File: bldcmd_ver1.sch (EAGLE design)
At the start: 26 parts, among them IC1 STSPIN32F0, Q1 PSMN2R4-30MLD, Q2 PSMN2R4-30MLD, Q3 PSMN2R4-30MLD, Q4 PSMN2R4-30MLD, Q5 PSMN2R4-30MLD, Q6 PSMN2R4-30MLD

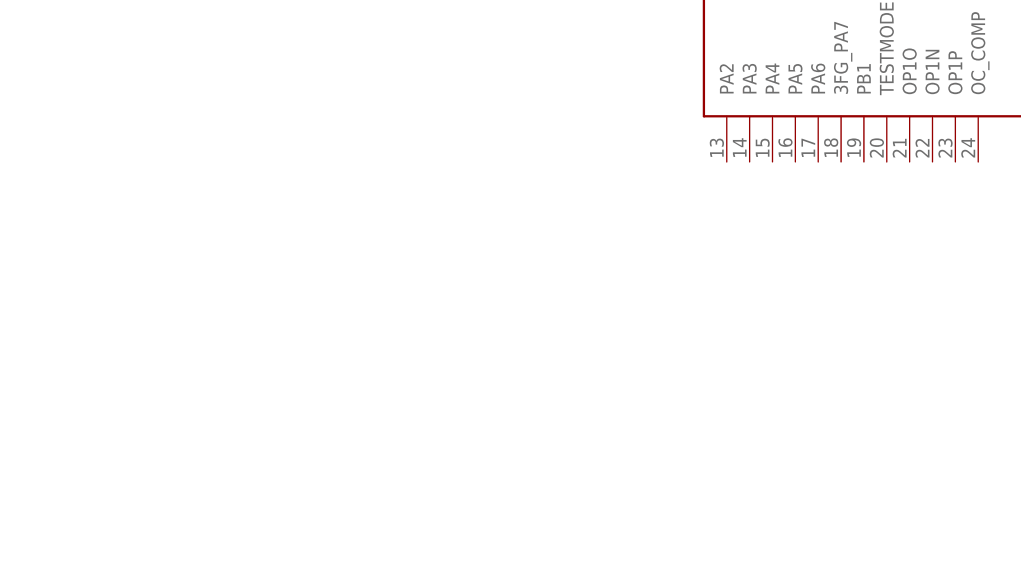
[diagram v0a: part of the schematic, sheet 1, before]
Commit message: 磁気エンコーダAS5047P追加
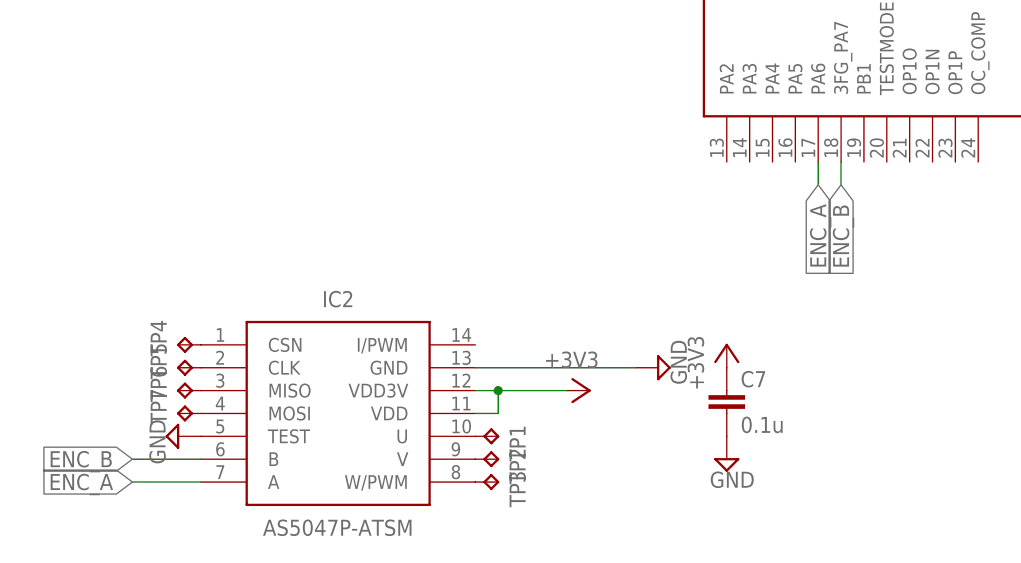
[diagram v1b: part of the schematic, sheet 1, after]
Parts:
- added C7: 0.1u, rcl:C-EUC0603K
- added IC2: AS5047P-ATSM, rcssl_lib:AS5047P-ATSM
- added TP1, TP2, TP3, TP4, TP5, TP6, TP7: TPTP06R, testpad:TPTP06R
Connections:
- new net +3V3: C7.1, IC2.VDD, IC2.VDD3V
- new net ENC_A: IC1.PA6, IC2.A
- new net ENC_B: IC1.3FG_PA7, IC2.B
- new net N$12: IC2.MISO, TP6.TP
- new net N$17: IC2.MOSI, TP7.TP
- new net N$2: IC2.U, TP1.TP
- new net N$3: IC2.V, TP2.TP
- new net N$6: IC2.W/PWM, TP3.TP
- new net N$7: IC2.CSN, TP4.TP
- new net N$8: IC2.CLK, TP5.TP
- net GND: now also C7.2, IC2.GND, IC2.TEST
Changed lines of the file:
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@@
 <part name="R13" library="rcl" library_urn="urn:adsk.eagle:library:334" deviceset="R-EU_" device="R3216" package3d_urn="urn:adsk.eagle:package:23557/2" value="0.01"/>
 <part name="SUPPLY1" library="supply2" library_urn="urn:adsk.eagle:library:372" deviceset="GND" device=""/>
+<part name="IC2" library="rcssl_lib" deviceset="AS5047P-ATSM" device=""/>
+<part name="+3V1" library="supply1" library_urn="urn:adsk.eagle:library:371" deviceset="+3V3" device=""/>
+<part name="SUPPLY2" library="supply2" library_urn="urn:adsk.eagle:library:372" deviceset="GND" device=""/>
+<part name="C7" library="rcl" library_urn="urn:adsk.eagle:library:334" deviceset="C-EU" device="C0603K" package3d_urn="urn:adsk.eagle:package:23680/2" value="0.1u"/>
+<part name="+3V2" library="supply1" library_urn="urn:adsk.eagle:library:371" deviceset="+3V3" device=""/>
+<part name="SUPPLY3" library="supply2" library_urn="urn:adsk.eagle:library:372" deviceset="GND" device=""/>
+<part name="TP1" library="testpad" library_urn="urn:adsk.eagle:library:385" deviceset="TP" device="TP06R" package3d_urn="urn:adsk.eagle:package:27954/1"/>
+<part name="TP2" library="testpad" library_urn="urn:adsk.eagle:library:385" deviceset="TP" device="TP06R" package3d_urn="urn:adsk.eagle:package:27954/1"/>
+<part name="TP3" library="testpad" library_urn="urn:adsk.eagle:library:385" deviceset="TP" device="TP06R" package3d_urn="urn:adsk.eagle:package:27954/1"/>
+<part name="TP4" library="testpad" library_urn="urn:adsk.eagle:library:385" deviceset="TP" device="TP06R" package3d_urn="urn:adsk.eagle:package:27954/1"/>
+<part name="TP5" library="testpad" library_urn="urn:adsk.eagle:library:385" deviceset="TP" device="TP06R" package3d_urn="urn:adsk.eagle:package:27954/1"/>
+<part name="TP6" library="testpad" library_urn="urn:adsk.eagle:library:385" deviceset="TP" device="TP06R" package3d_urn="urn:adsk.eagle:package:27954/1"/>
+<part name="TP7" library="testpad" library_urn="urn:adsk.eagle:library:385" deviceset="TP" device="TP06R" package3d_urn="urn:adsk.eagle:package:27954/1"/>
+<part name="SUPPLY4" library="supply2" library_urn="urn:adsk.eagle:library:372" deviceset="GND" device=""/>
 </parts>
 <sheets>
@@
 <instance part="C2" gate="G$1" x="58.42" y="-12.7" rot="R90"/>
 <instance part="C3" gate="G$1" x="58.42" y="-22.86" rot="R90"/>
+<instance part="IC2" gate="G$1" x="-43.18" y="-71.12"/>
+<instance part="+3V1" gate="G$1" x="0" y="-76.2" rot="R270"/>
+<instance part="SUPPLY2" gate="GND" x="7.62" y="-73.66" rot="R90"/>
+<instance part="C7" gate="G$1" x="15.24" y="-76.2"/>
+<instance part="+3V2" gate="G$1" x="15.24" y="-71.12"/>
+<instance part="SUPPLY3" gate="GND" x="15.24" y="-83.82"/>
+<instance part="TP1" gate="G$1" x="-10.16" y="-81.28" rot="R270"/>
+<instance part="TP2" gate="G$1" x="-10.16" y="-83.82" rot="R270"/>
+<instance part="TP3" gate="G$1" x="-10.16" y="-86.36" rot="R270"/>
+<instance part="TP4" gate="G$1" x="-45.72" y="-71.12" rot="R90"/>
+<instance part="TP5" gate="G$1" x="-45.72" y="-73.66" rot="R90"/>
+<instance part="TP6" gate="G$1" x="-45.72" y="-76.2" rot="R90"/>
+<instance part="TP7" gate="G$1" x="-45.72" y="-78.74" rot="R90"/>
+<instance part="SUPPLY4" gate="GND" x="-45.72" y="-81.28" rot="R270"/>
 </instances>
 <busses>
@@
 </segment>
 </net>
+<net name="GND" class="0">
+<segment>
+<pinref part="IC2" gate="G$1" pin="GND"/>
+<pinref part="SUPPLY2" gate="GND" pin="GND"/>
+<wire x1="-12.7" y1="-73.66" x2="5.08" y2="-73.66" width="0.1524" layer="91"/>
+</segment>
+<segment>
+<pinref part="C7" gate="G$1" pin="2"/>
+<pinref part="SUPPLY3" gate="GND" pin="GND"/>
+</segment>
+<segment>
+<pinref part="IC2" gate="G$1" pin="TEST"/>
+<pinref part="SUPPLY4" gate="GND" pin="GND"/>
+</segment>
+</net>
+<net name="+3V3" class="0">
+<segment>
+<pinref part="IC2" gate="G$1" pin="VDD"/>
+<wire x1="-12.7" y1="-78.74" x2="-10.16" y2="-78.74" width="0.1524" layer="91"/>
+<wire x1="-10.16" y1="-78.74" x2="-10.16" y2="-76.2" width="0.1524" layer="91"/>
+<pinref part="IC2" gate="G$1" pin="VDD3V"/>
+<wire x1="-10.16" y1="-76.2" x2="-12.7" y2="-76.2" width="0.1524" layer="91"/>
+<pinref part="+3V1" gate="G$1" pin="+3V3"/>
+<wire x1="-10.16" y1="-76.2" x2="-2.54" y2="-76.2" width="0.1524" layer="91"/>
+<junction x="-10.16" y="-76.2"/>
+</segment>
+<segment>
+<pinref part="C7" gate="G$1" pin="1"/>
+<pinref part="+3V2" gate="G$1" pin="+3V3"/>
+</segment>
+</net>
+<net name="ENC_B" class="0">
+<segment>
+<pinref part="IC2" gate="G$1" pin="B"/>
+<wire x1="-43.18" y1="-83.82" x2="-50.8" y2="-83.82" width="0.1524" layer="91"/>
+<label x="-50.8" y="-83.82" size="1.778" layer="95" rot="R180" xref="yes"/>
+</segment>
+<segment>
+<pinref part="IC1" gate="G$1" pin="3FG_PA7"/>
+<wire x1="27.94" y1="-50.8" x2="27.94" y2="-53.34" width="0.1524" layer="91"/>
+<label x="27.94" y="-53.34" size="1.778" layer="95" rot="R270" xref="yes"/>
+</segment>
+</net>
+<net name="ENC_A" class="0">
+<segment>
+<pinref part="IC2" gate="G$1" pin="A"/>
+<wire x1="-43.18" y1="-86.36" x2="-50.8" y2="-86.36" width="0.1524" layer="91"/>
+<label x="-50.8" y="-86.36" size="1.778" layer="95" rot="R180" xref="yes"/>
+</segment>
+<segment>
+<pinref part="IC1" gate="G$1" pin="PA6"/>
+<wire x1="25.4" y1="-50.8" x2="25.4" y2="-53.34" width="0.1524" layer="91"/>
+<label x="25.4" y="-53.34" size="1.778" layer="95" rot="R270" xref="yes"/>
+</segment>
+</net>
+<net name="N$2" class="0">
+<segment>
+<pinref part="IC2" gate="G$1" pin="U"/>
+<pinref part="TP1" gate="G$1" pin="TP"/>
+</segment>
+</net>
+<net name="N$3" class="0">
+<segment>
+<pinref part="IC2" gate="G$1" pin="V"/>
+<pinref part="TP2" gate="G$1" pin="TP"/>
+</segment>
+</net>
+<net name="N$6" class="0">
+<segment>
+<pinref part="IC2" gate="G$1" pin="W/PWM"/>
+<pinref part="TP3" gate="G$1" pin="TP"/>
+</segment>
+</net>
+<net name="N$7" class="0">
+<segment>
+<pinref part="IC2" gate="G$1" pin="CSN"/>
+<pinref part="TP4" gate="G$1" pin="TP"/>
+</segment>
+</net>
+<net name="N$8" class="0">
+<segment>
+<pinref part="IC2" gate="G$1" pin="CLK"/>
+<pinref part="TP5" gate="G$1" pin="TP"/>
+</segment>
+</net>
+<net name="N$12" class="0">
+<segment>
+<pinref part="IC2" gate="G$1" pin="MISO"/>
+<pinref part="TP6" gate="G$1" pin="TP"/>
+</segment>
+</net>
+<net name="N$17" class="0">
+<segment>
+<pinref part="IC2" gate="G$1" pin="MOSI"/>
+<pinref part="TP7" gate="G$1" pin="TP"/>
+</segment>
+</net>

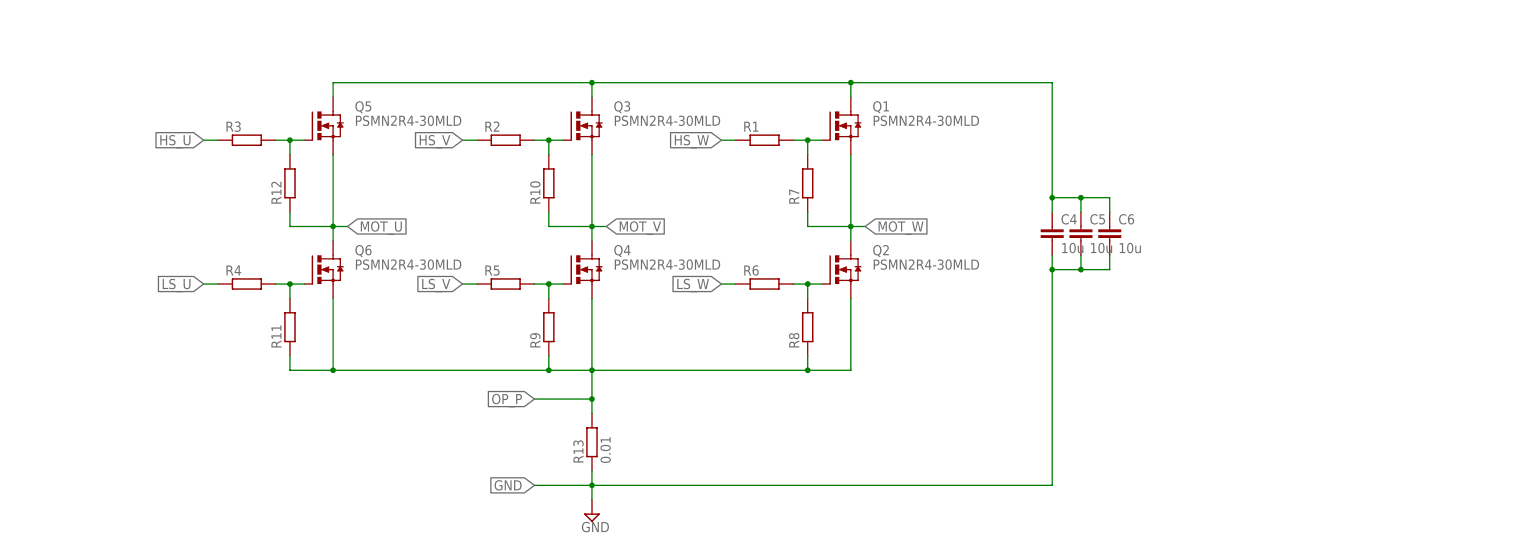
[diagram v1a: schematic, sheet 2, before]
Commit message: CスナバをGNDからローサイドFETのソースに接続変更
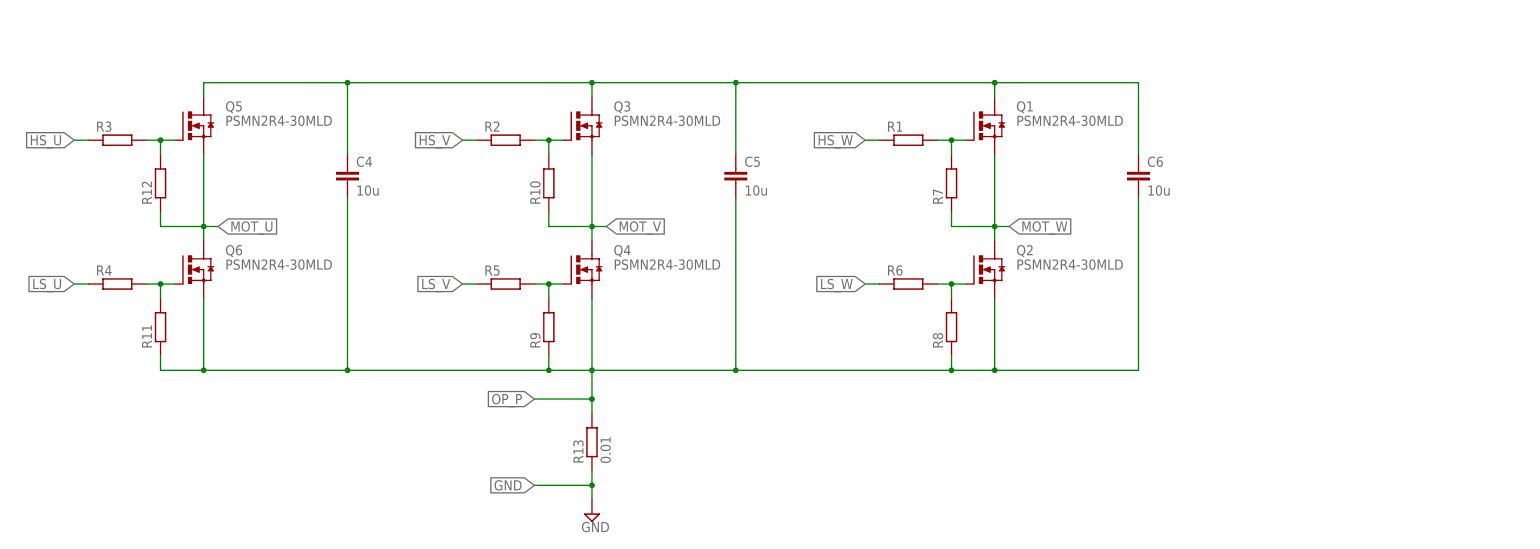
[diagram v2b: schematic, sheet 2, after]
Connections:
- net GND: no longer C4.2, C5.2, C6.2
- net OP_P: now also C4.2, C5.2, C6.2
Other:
- moved on the sheet: C4, C5, C6, Q1, Q2, Q5, Q6, R1, R11, R12, R3, R4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
